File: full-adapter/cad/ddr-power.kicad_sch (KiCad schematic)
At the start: 67 parts, among them U1 RK3568B2, U2 H5TQ4G63EFR-RDC, U3 H5TQ4G63EFR-RDC

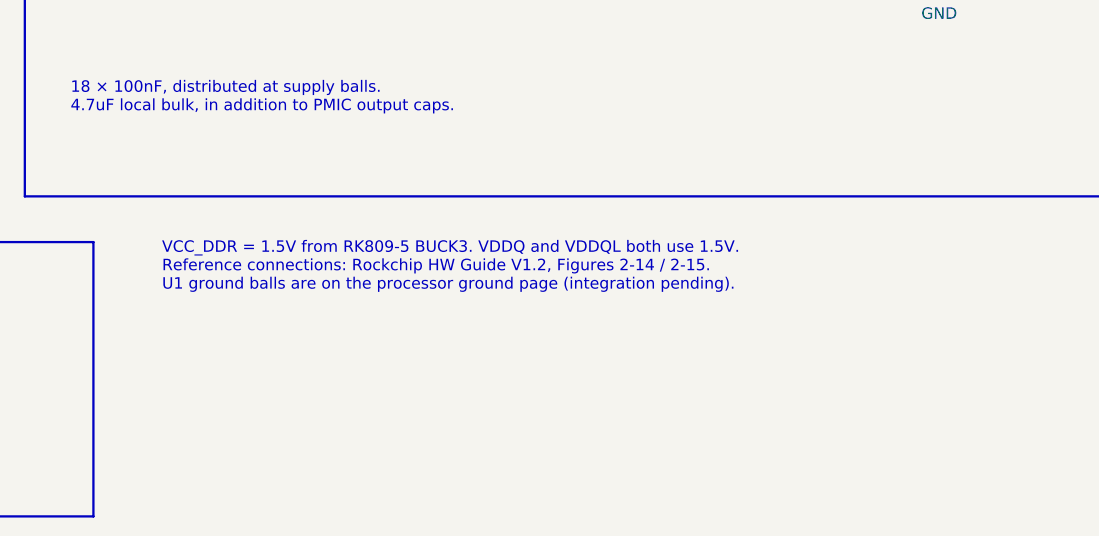
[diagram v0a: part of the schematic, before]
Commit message: cad: capture processor core bypass and all 208 ground balls
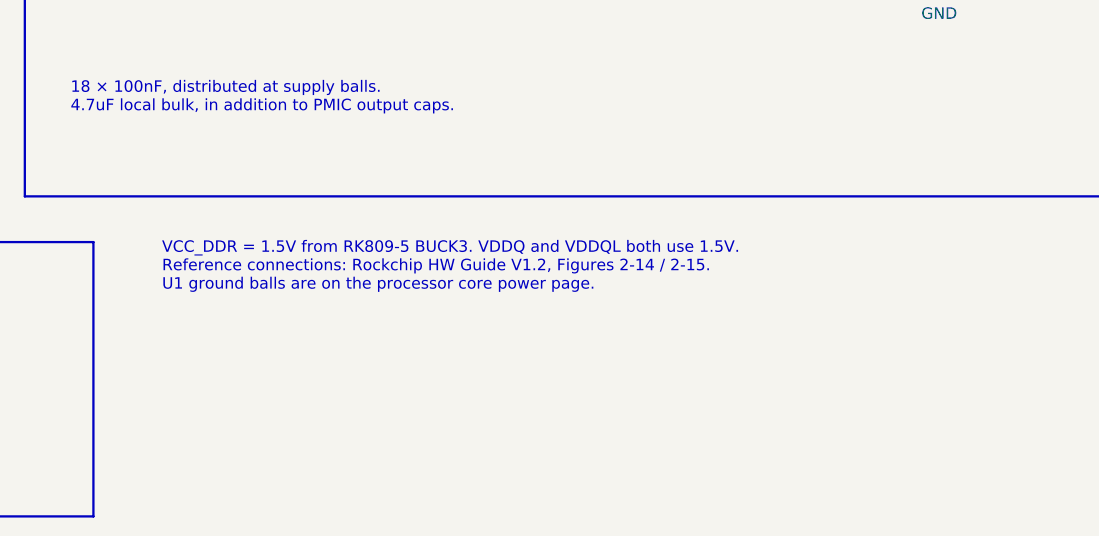
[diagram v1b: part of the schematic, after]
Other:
- note added: "VCC_DDR = 1.5V from RK809-5 BUCK3. VDDQ and VDDQL both use 1.5V. Reference connections: Rockchip HW Guide V1.2, Figures 2-14 / 2-15. U1 ground balls are on the processor core power page."
- note removed: "VCC_DDR = 1.5V from RK809-5 BUCK3. VDDQ and VDDQL both use 1.5V. Reference connections: Rockchip HW Guide V1.2, Figures 2-14 / 2-15. U1 ground balls are on the processor ground page (integration pending)."
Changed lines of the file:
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@@
 (property "Description" "Power symbol creates a global label with name \"GND\" , ground" (at 121.92 279.4 0) (effects (font (size 1.27 1.27))) (hide yes))
 (pin "1")(instances (project "full-adapter" (path "/fda20879-fa66-56c0-be14-de2506349b46/dec2022a-299e-5efb-80b8-8fb12375090e" (reference "#PWRddrpower027") (unit 1)))))
-(text "VCC_DDR = 1.5V from RK809-5 BUCK3. VDDQ and VDDQL both use 1.5V.\nReference connections: Rockchip HW Guide V1.2, Figures 2-14 / 2-15.\nU1 ground balls are on the processor ground page (integration pending)." (at 162.56 251.46 0) (effects (font (size 1.27 1.27)) (justify left top)))
+(text "VCC_DDR = 1.5V from RK809-5 BUCK3. VDDQ and VDDQL both use 1.5V.\nReference connections: Rockchip HW Guide V1.2, Figures 2-14 / 2-15.\nU1 ground balls are on the processor core power page." (at 162.56 251.46 0) (effects (font (size 1.27 1.27)) (justify left top)))
 )
